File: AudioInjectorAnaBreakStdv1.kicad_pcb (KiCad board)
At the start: 2 copper layers, 100 x 41.5 mm, 4 parts, among them J1 Conn_02x03

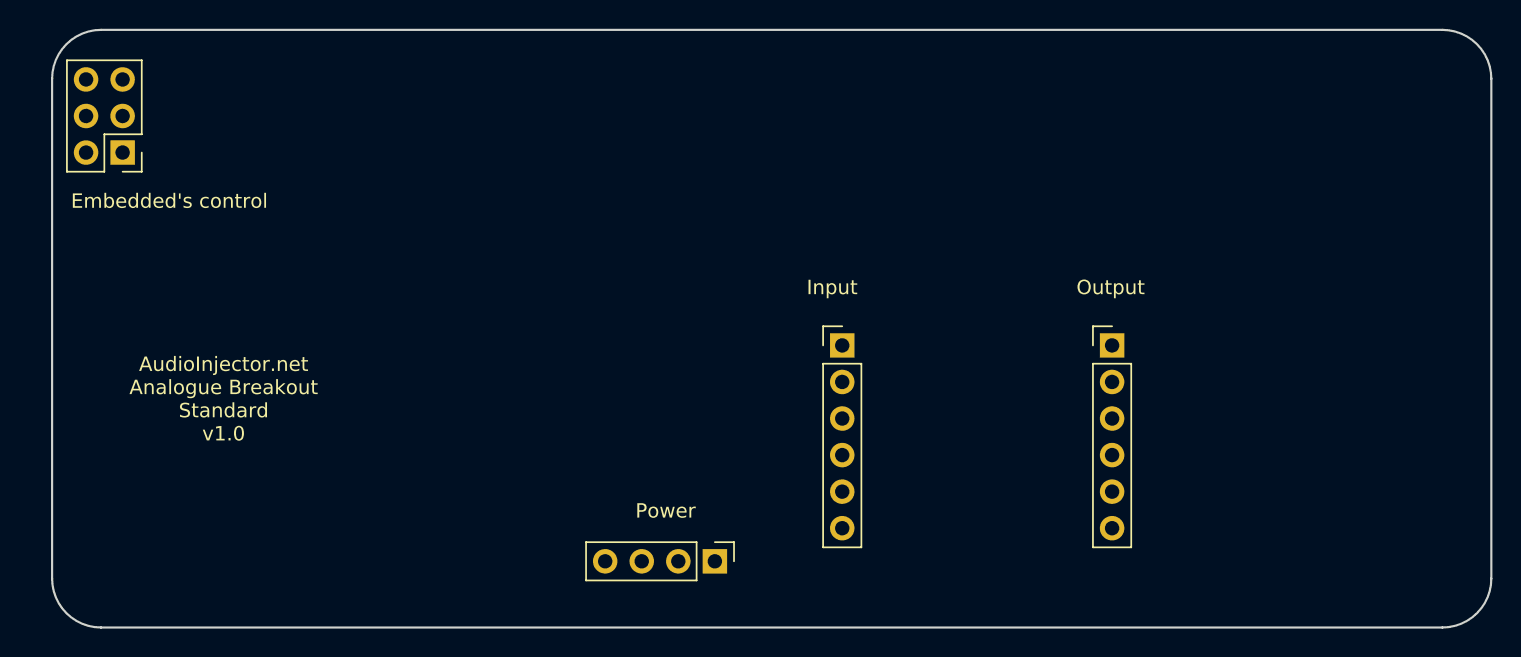
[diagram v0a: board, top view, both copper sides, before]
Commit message: Updated footprints and made sure net export/import was working
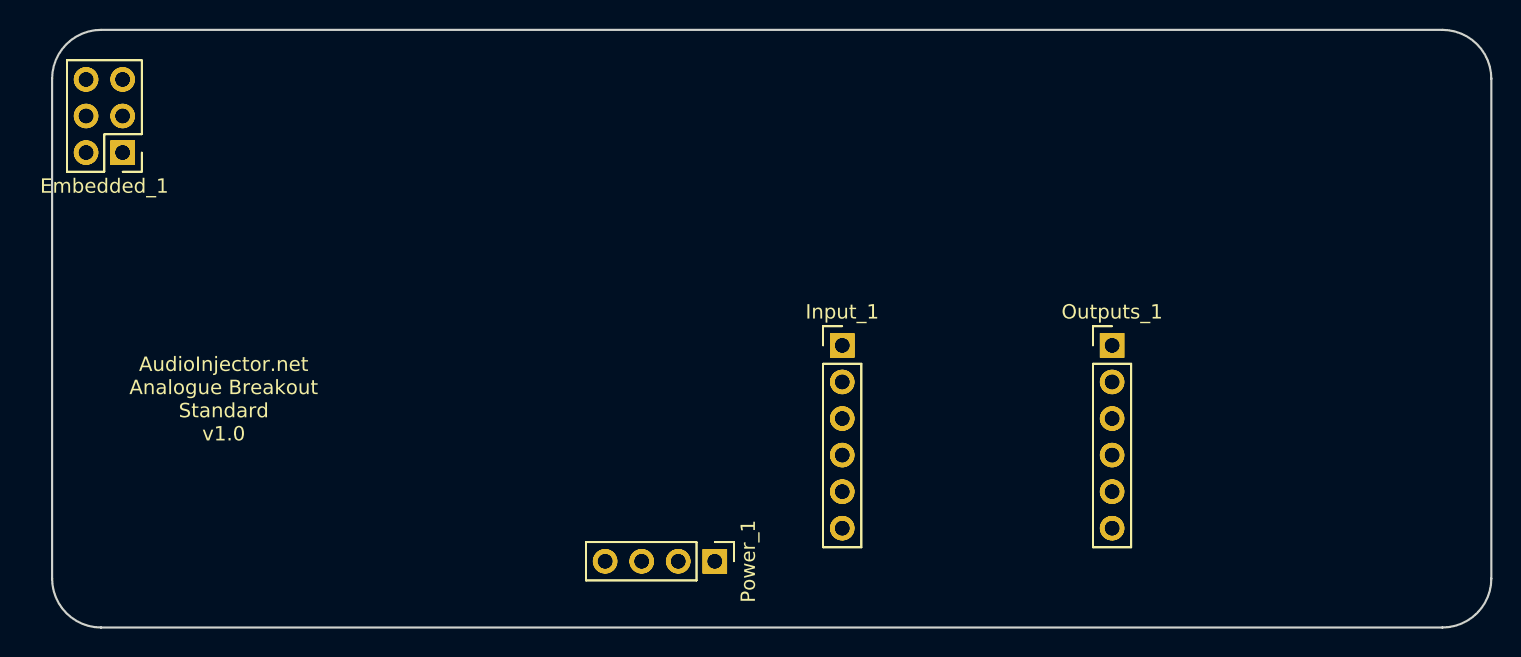
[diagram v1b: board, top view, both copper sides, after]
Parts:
- added Embedded_1: Embedded, Connector_PinHeader_2.54mm:PinHeader_2x03_P2.54mm_Vertical, F.Cu at (74.3, 128.8)
- added Input_1: IN, Connector_PinHeader_2.54mm:PinHeader_1x06_P2.54mm_Vertical, F.Cu at (124.3, 142.2)
- added Outputs_1: OUT, Connector_PinHeader_2.54mm:PinHeader_1x06_P2.54mm_Vertical, F.Cu at (143.1, 142.2)
- added Power_1: Power, Connector_PinHeader_2.54mm:PinHeader_1x04_P2.54mm_Vertical, F.Cu at (115.4, 157.2)
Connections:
- J1 pad 1: V5 -> (no net)
- J1 pad 5: /Codec/~mute_logic -> (no net)
- L_G_R_OUT_1 pad 1: /Codec/BMUTEC -> (no net)
- L_G_R_OUT_1 pad 2: /Codec/AOUTB- -> (no net)
- L_G_R_OUT_1 pad 3: /Codec/AOUTB+ -> (no net)
- L_G_R_OUT_1 pad 4: /Codec/AOUTA+ -> (no net)
- L_G_R_OUT_1 pad 5: /Codec/AOUTA- -> (no net)
- L_G_R_OUT_1 pad 6: /Codec/AMUTEC -> (no net)
- L_G_R_OUT_2 pad 1: /Codec/AINB- -> (no net)
- L_G_R_OUT_2 pad 2: /Codec/AINB+ -> (no net)
- L_G_R_OUT_2 pad 4: /Codec/AINA- -> (no net)
- L_G_R_OUT_2 pad 5: /Codec/AINA+ -> (no net)
- V12s_1 pad 1: /Codec/Vph -> (no net)
- V12s_1 pad 2: /Codec/V12 -> (no net)
- V12s_1 pad 4: /Codec/V-12 -> (no net)
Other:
- board text removed: "Embedded's control"
- board text removed: "Input"
- board text removed: "Output"
- board text removed: "Power"

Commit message: Shifted footprints - pre settling v1.0
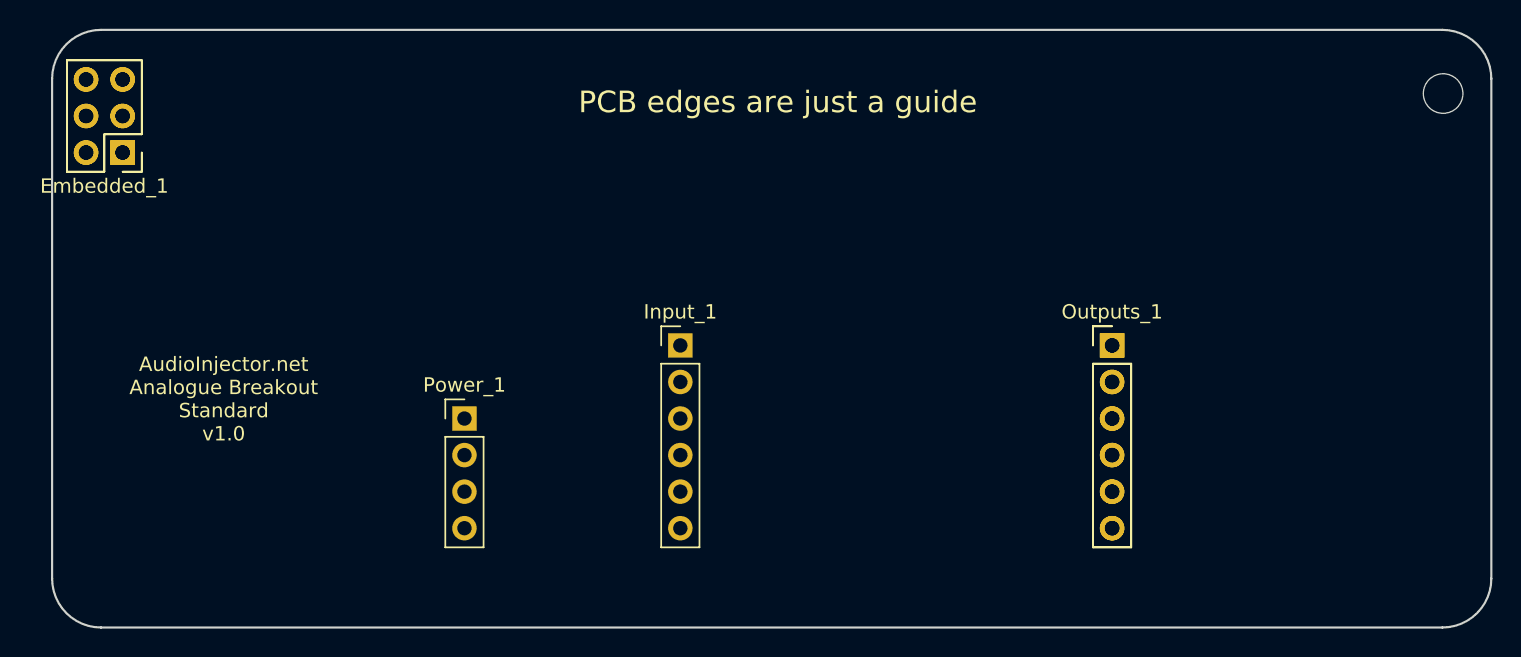
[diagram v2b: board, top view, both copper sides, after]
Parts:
- removed L_G_R_OUT_2: OUT, Connector_PinHeader_2.54mm:PinHeader_1x06_P2.54mm_Vertical
- removed V12s_1: OUT, Connector_PinHeader_2.54mm:PinHeader_1x04_P2.54mm_Vertical
- added ?: , RPi:RPi_Hat_Mounting_Hole, F.Cu at (166.1, 124.7)
- moved Power_1 20.0 mm to (98.0, 147.3), turned to 0 degrees
- moved Input_1 11.2 mm to (113.0, 142.2)
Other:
- board text added: "PCB edges are just a guide"

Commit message: v1.0, pre-freeze. Flipped headers to back.
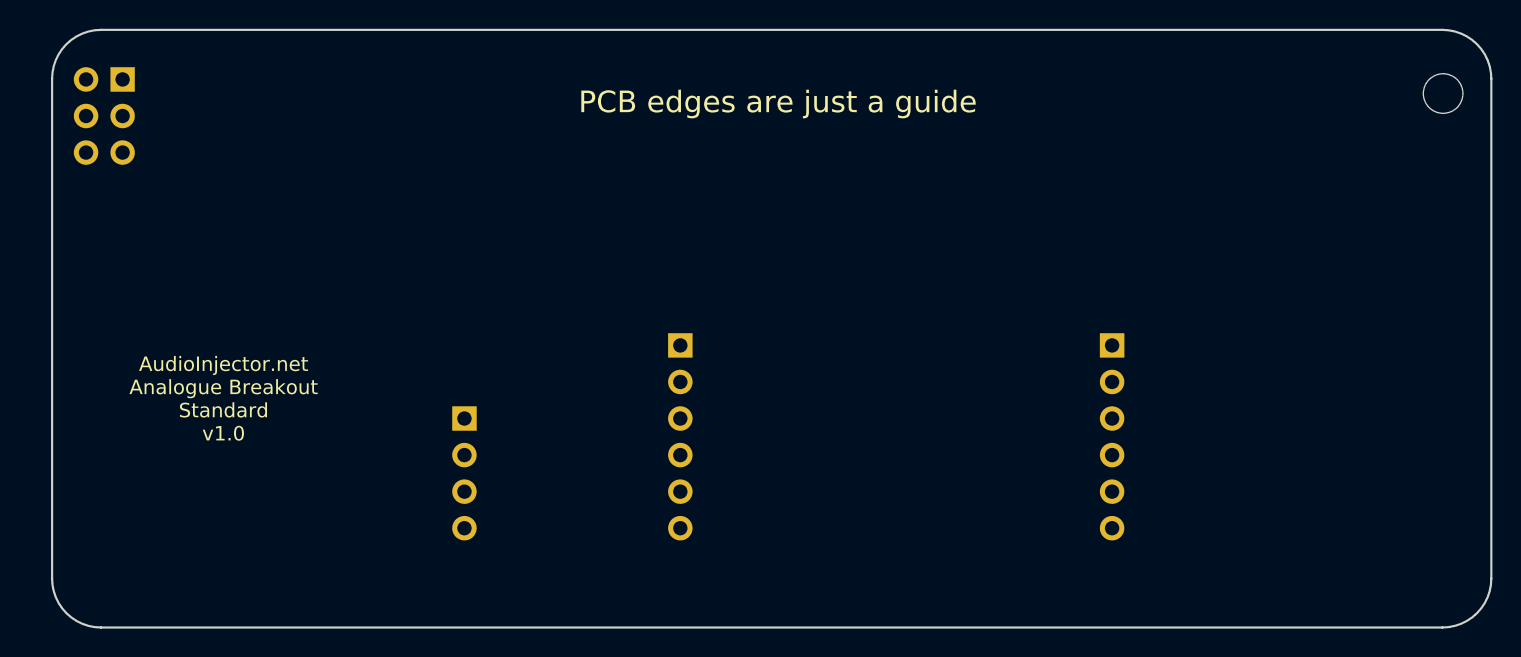
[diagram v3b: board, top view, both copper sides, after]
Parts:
- removed J1: Conn_02x03, Connector_PinHeader_2.54mm:PinHeader_2x03_P2.54mm_Vertical
- removed L_G_R_OUT_1: OUT, Connector_PinHeader_2.54mm:PinHeader_1x06_P2.54mm_Vertical
- Embedded_1, Input_1, Outputs_1, Power_1: moved to B.Cu
- moved Embedded_1 5.08 mm to (74.3, 123.7)
- turned Input_1 to 180 degrees
- turned Outputs_1 to 180 degrees
- turned Power_1 to 180 degrees
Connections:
- Embedded_1 pad 2: GPIO4 -> (no net)
- Embedded_1 pad 4: GPIO14 -> (no net)
- Embedded_1 pad 6: GPIO15 -> (no net)
- Power_1 pad 2: (no net) -> GND
- Power_1 pad 3: GND -> (no net)
